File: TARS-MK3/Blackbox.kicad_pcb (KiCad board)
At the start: 2 copper layers, 50.8 x 22.9 mm, 46 parts, among them J1 RP Header 16 pin, J2 RP Header 12 pin, J3 Micro_SD_Card, J4 USB_B_Micro, U1 H3LIS331DL, U2 LSM9DS1, U3 RP2040_chip, U4 MS5611-01BA, Y1 Crystal_GND24

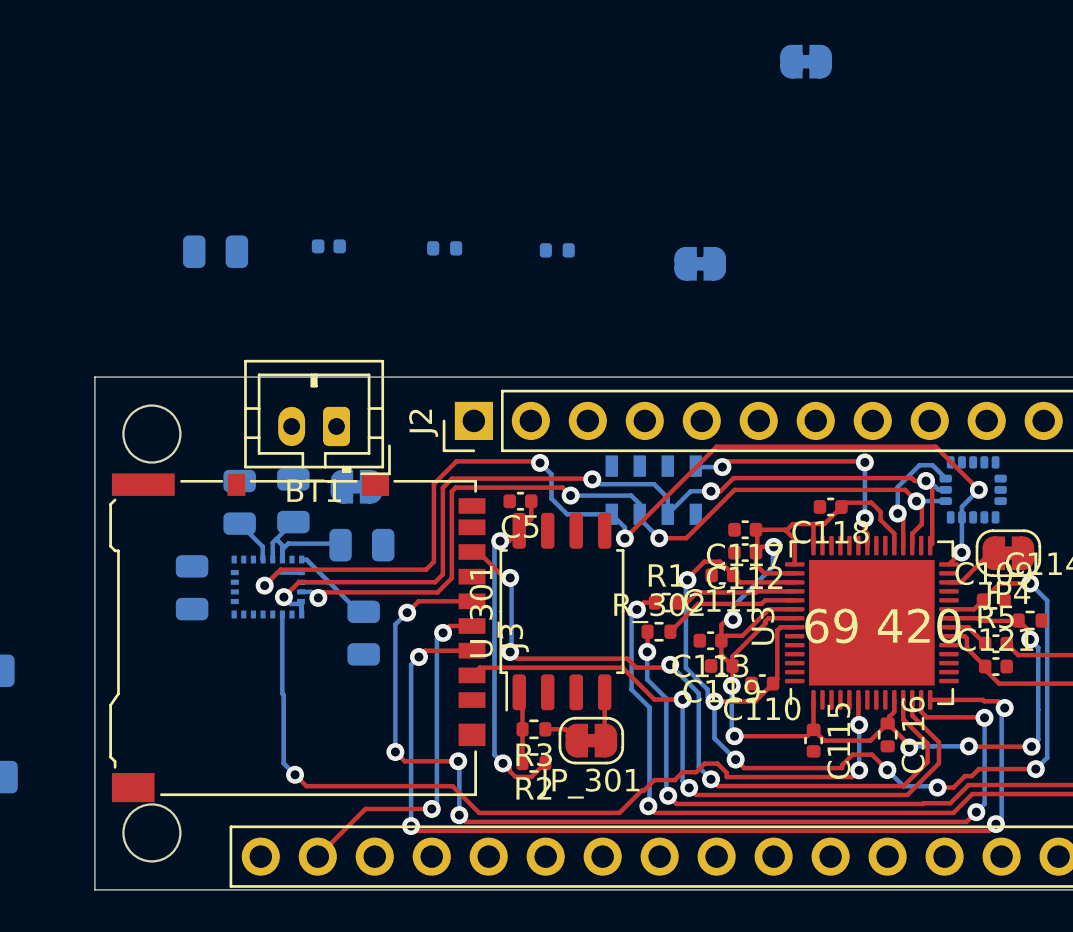
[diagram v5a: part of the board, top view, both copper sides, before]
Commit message: worked on bbx routing
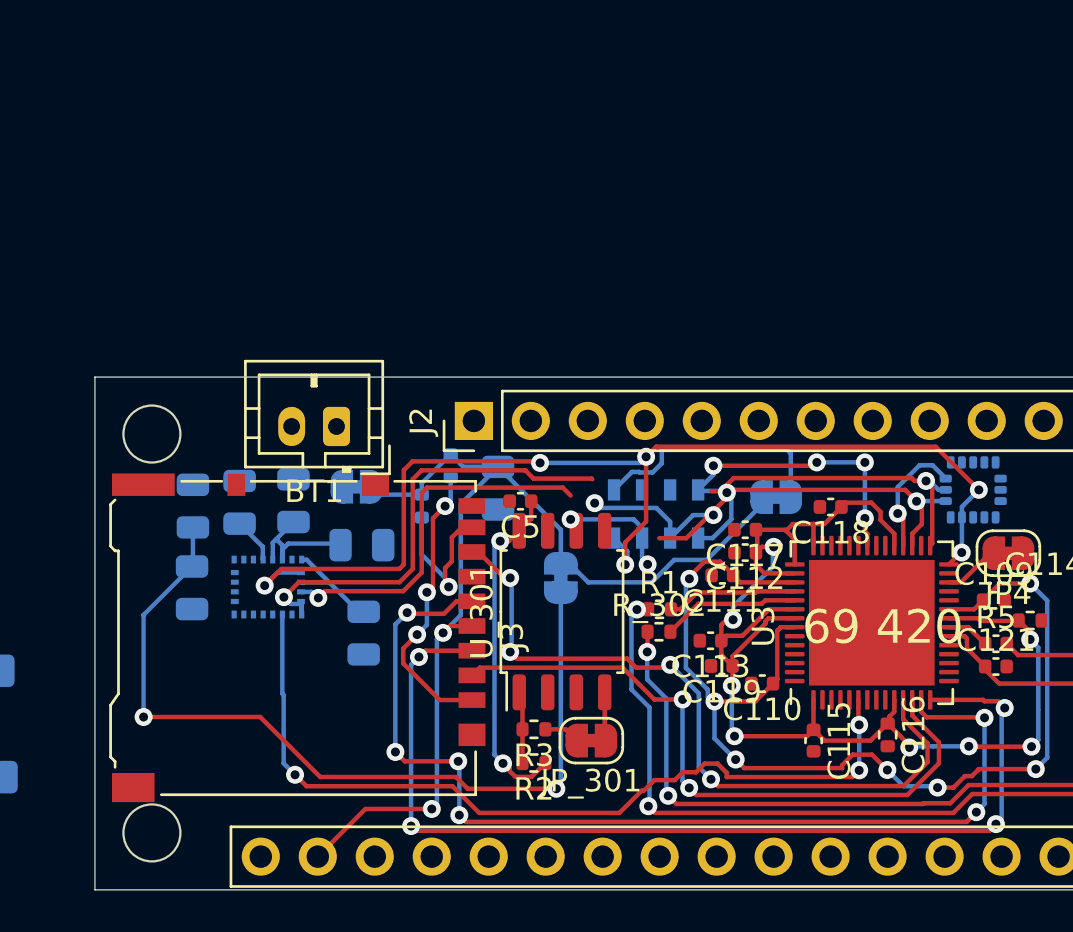
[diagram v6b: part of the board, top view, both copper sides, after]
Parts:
- C122: footprint Capacitor_SMD:C_0402_1005Metric -> Capacitor_SMD:C_0805_2012Metric
- moved JP1 19.5 mm to (170.8, 100.4), turned to 0 degrees
- moved JP2 15.3 mm to (161.2, 104.0), turned to -90 degrees
- moved C122 13.2 mm to (158.4, 100.0), turned to 90 degrees
- moved R101 11.5 mm to (155.0, 100.8), turned to -90 degrees
- moved C103 11.4 mm to (144.8, 100.8), turned to 90 degrees
- moved R102 10.7 mm to (156.3, 99.0), turned to -90 degrees
- moved U4 1.07 mm to (165.4, 101.2)
- moved R1 0.42 mm to (165.6, 105.4)
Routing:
- net Net-(C102-Pad1): track 0.00 -> 38.3 mm, vias 0 -> 2
- net /3V3: track 15.4 -> 47.7 mm
- net Net-(J3-Pad1): track 0.00 -> 12.9 mm, vias 0 -> 3
- net Net-(C101-Pad2): track 0.00 -> 11.1 mm
- net Net-(J3-Pad8): track 0.00 -> 6.60 mm, vias 0 -> 1
- net /MS5611_CS: track 11.4 -> 16.3 mm, vias 3 -> 5
- net /SNS_SPI_SCK: track 46.7 -> 50.0 mm, vias 5 -> 6

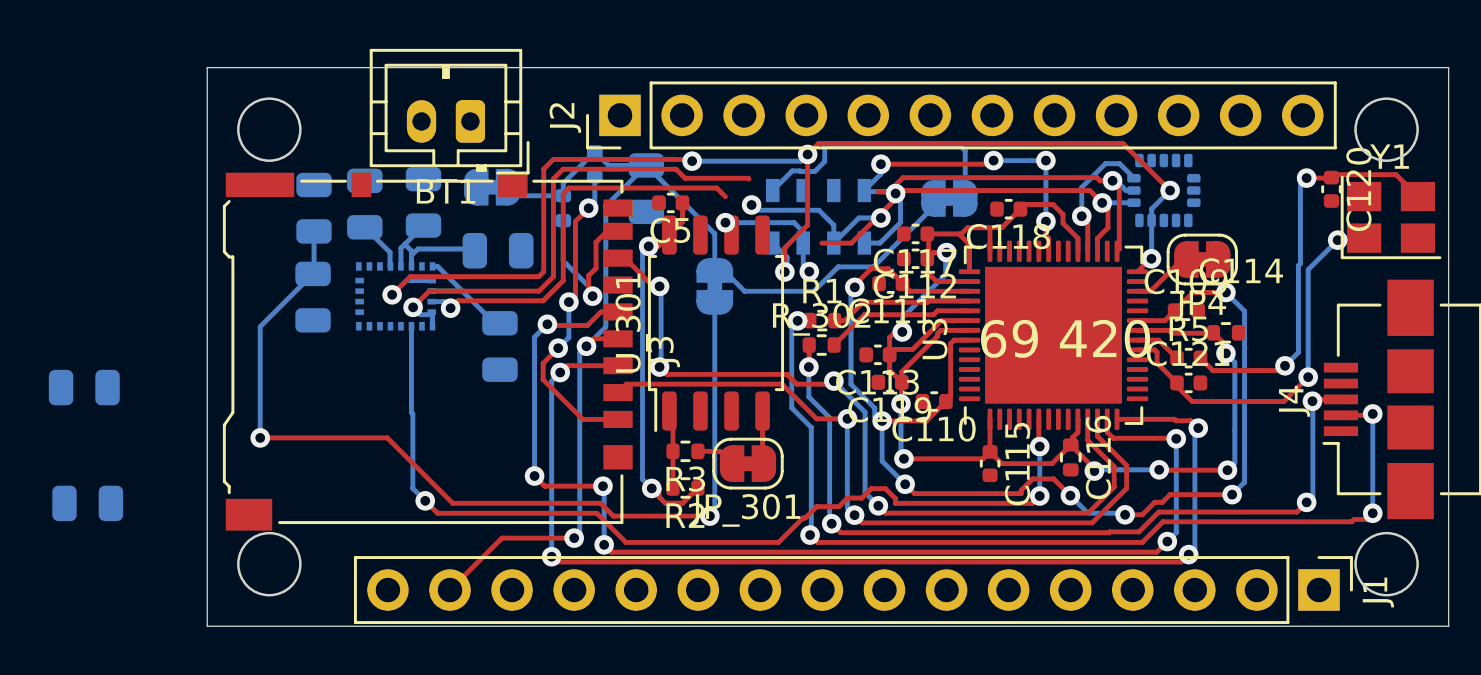
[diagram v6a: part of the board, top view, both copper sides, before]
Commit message: Blackbox PCB updates
PCB done, ready to be reviewed. Just needs linear regulator and memes ofc.
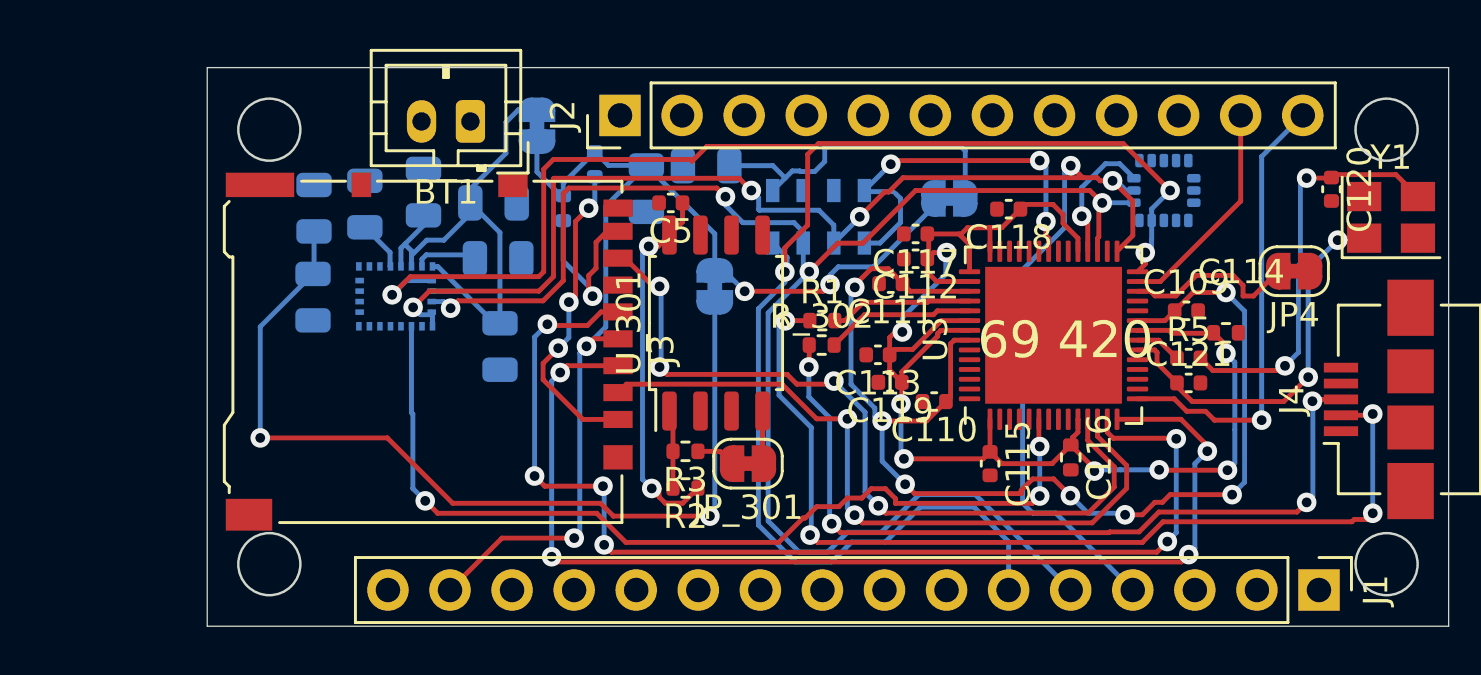
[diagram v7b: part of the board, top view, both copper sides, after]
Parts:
- moved C101 27.0 mm to (160.8, 99.1), turned to 0 degrees
- moved C108 19.6 mm to (152.3, 102.9), turned to 0 degrees
- moved JP4 3.79 mm to (184.9, 103.4)
- moved JP3 3.11 mm to (153.9, 97.4), turned to 90 degrees
- moved C105 1.96 mm to (152.1, 100.6)
- moved C106 0.42 mm to (149.3, 100.1)
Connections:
- U3 pad 15: /MS5611_CS -> /I2C1_SDA
- U3 pad 16: /H3LIS331DL_CS -> unconnected-(U3-Pad16)
- U3 pad 17: /LSM9_CS_M -> unconnected-(U3-Pad17)
- U3 pad 27: /MS5611_CS -> /I2C0_SCL
- U3 pad 7: /I2C0_SCL -> /MS5611_CS
- U3 pad 8: /I2C1_SDA -> unconnected-(U3-Pad8)
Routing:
- net /SNS_SPI_MOSI: track 37.7 -> 65.7 mm
- net /SNS_SPI_SCK: track 50.0 -> 75.6 mm, vias 6 -> 4
- net /SNS_SPI_MISO: track 41.3 -> 64.0 mm, vias 4 -> 5
- net /I2C1_SDA: track 0.00 -> 18.6 mm, vias 0 -> 1
- net Net-(C104-Pad1): track 10.6 -> 22.5 mm
- net /I2C0_SCL: track 0.00 -> 9.09 mm
- net Net-(JP4-Pad2): track 2.54 -> 7.21 mm
- net (no net): track 0.00 -> 4.23 mm
- net Net-(C108-Pad1): track 0.00 -> 2.60 mm
- net Net-(C101-Pad2): track 11.1 -> 13.5 mm
- net /USB_D-: track 38.8 -> 39.5 mm
- net /3V3: track 47.7 -> 48.2 mm, vias 2 -> 4
- net /MS5611_CS: track 16.3 -> 15.9 mm, vias 5 -> 3

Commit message: blackbox memes
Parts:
- added G***: LOGO, memes:dogs, F.Cu at (181.0, 100.5)
- added G***: LOGO, memes:heart, F.Cu at (184.2, 111.3)
- added G***: LOGO, memes:duck, F.Cu at (183.8, 100.2)
- added G***: LOGO, memes:griddy, F.Cu at (165.8, 100.1)
- added G***: LOGO, memes:blackbox family, F.Cu at (166.3, 110.7)
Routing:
- net /SNS_SPI_SCK: track 75.6 -> 74.9 mm
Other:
- board text added: "Arna"
- board text added: "Daniel"
- board text added: "Eisha"
- board text added: "Rohini"
- board text added: "rip sam"
